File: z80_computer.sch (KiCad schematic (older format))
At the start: 14 parts, among them SW0 SW_Push, U0 Z80CPU, U1 CY62256NLL-55SNXI, U2 AT28C256_40PIN_ZIF, U4 SN74LS04N, U5 SN74LS00N, Y0 Crystal 6 MHZ

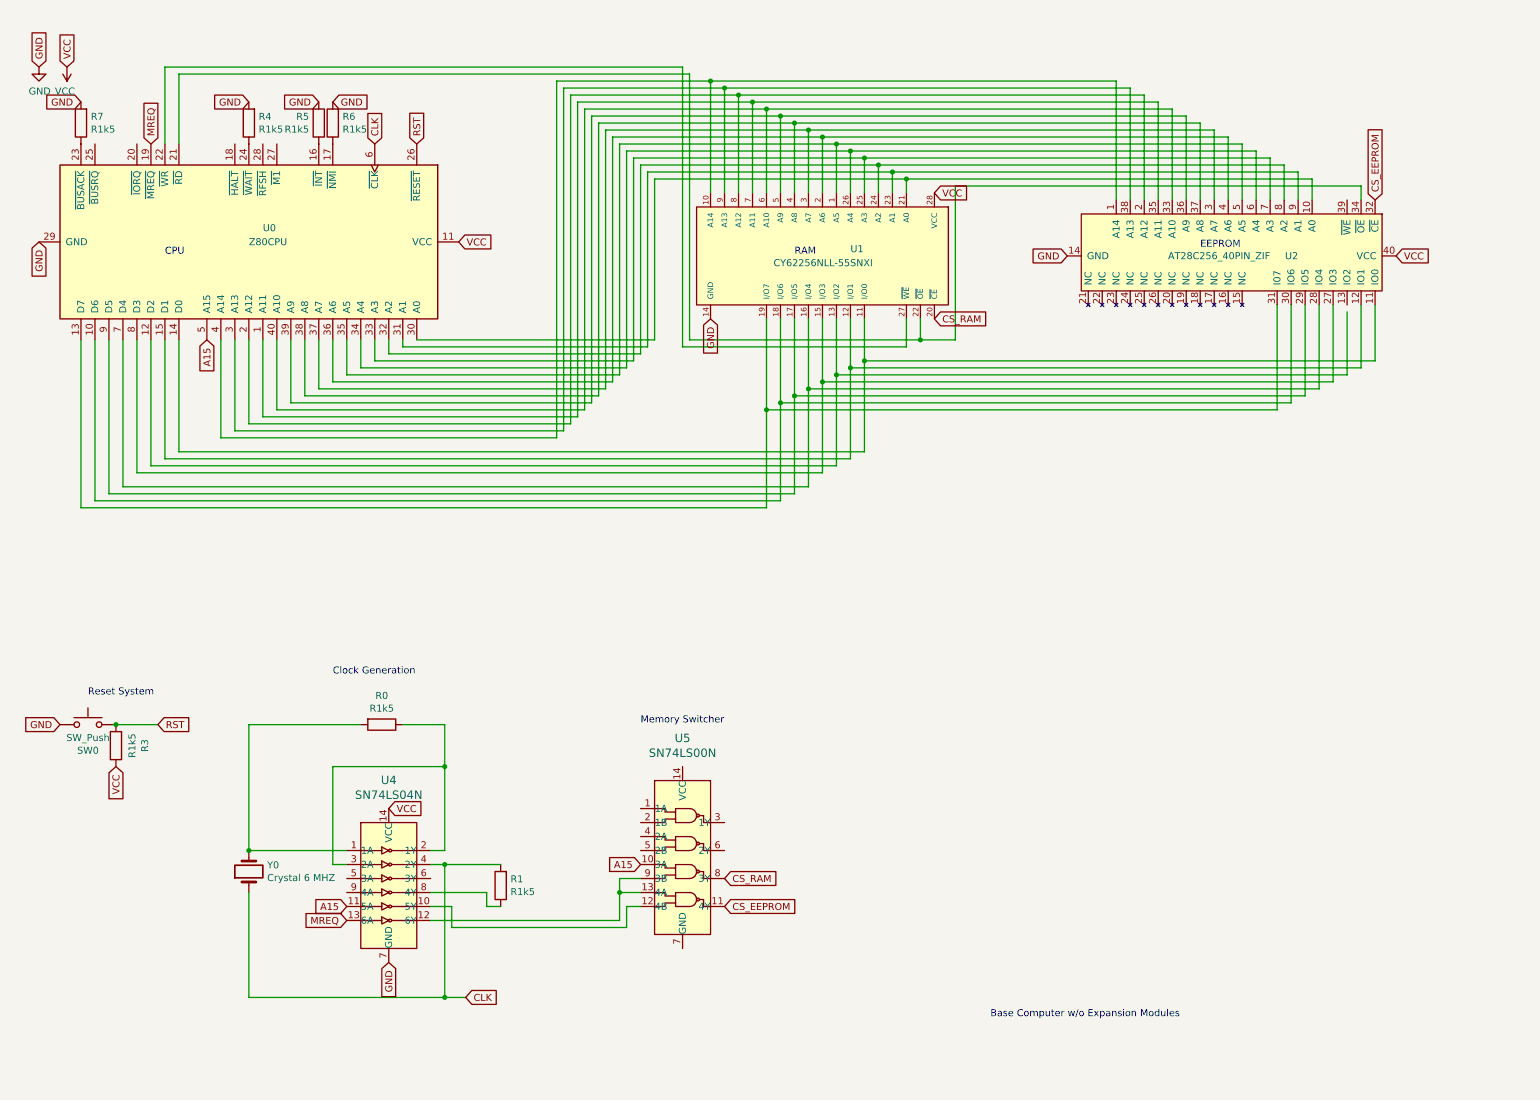
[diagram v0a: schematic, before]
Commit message: added second page on schematic detailing the debugging platform
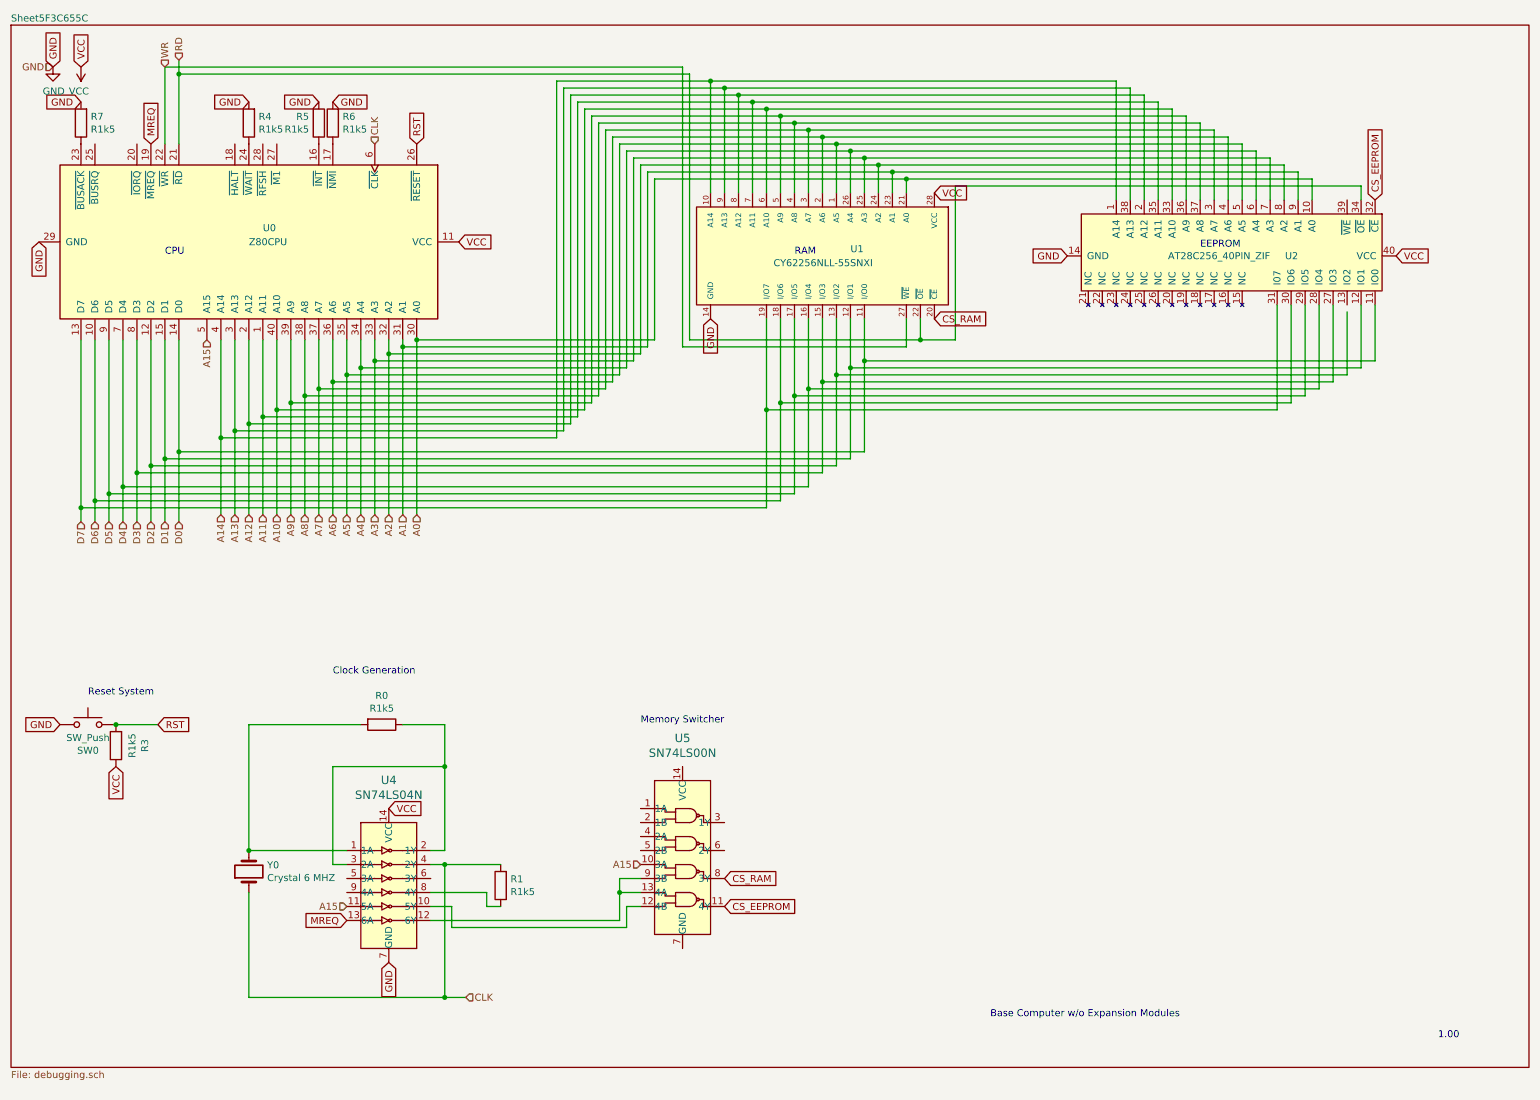
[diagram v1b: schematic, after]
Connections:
- net A14: now reaches U0.4 (A14), U1.10 (A14), U2.1 (A14)
- net A0: now reaches U0.30 (A0), U1.21 (A0), U2.10 (A0)
- net D0: now reaches U0.14 (D0), U1.11 (I/O0), U2.11 (IO0)
- net D1: now reaches U0.15 (D1), U1.12 (I/O1), U2.12 (IO1)
- net A12: now reaches U0.2 (A12), U1.8 (A12), U2.2 (A12)
- net D3: now reaches U0.8 (D3), U1.15 (I/O3), U2.27 (IO3)
- net D4: now reaches U0.7 (D4), U1.16 (I/O4), U2.28 (IO4)
- net D5: now reaches U0.9 (D5), U1.17 (I/O5), U2.29 (IO5)
- net A7: now reaches U0.37 (A7), U1.3 (A7), U2.3 (A7)
- net D6: now reaches U0.10 (D6), U1.18 (I/O6), U2.30 (IO6)
- net D7: now reaches U0.13 (D7), U1.19 (I/O7), U2.31 (I07)
- net A10: now reaches U0.40 (A10), U1.6 (A10), U2.33 (A10)
- net RD: now reaches U0.21 (~RD~), U1.22 (~OE~), U2.34 (~OE)
- net A11: now reaches U0.1 (A11), U1.7 (A11), U2.35 (A11)
- net A9: now reaches U0.39 (A9), U1.5 (A9), U2.36 (A9)
- net A8: now reaches U0.38 (A8), U1.4 (A8), U2.37 (A8)
- net A13: now reaches U0.3 (A13), U1.9 (A13), U2.38 (A13)
- net A6: now reaches U0.36 (A6), U1.2 (A6), U2.4 (A6)
- net A5: now reaches U0.35 (A5), U1.1 (A5), U2.5 (A5)
- net A4: now reaches U0.34 (A4), U1.26 (A4), U2.6 (A4)
- net A3: now reaches U0.33 (A3), U1.25 (A3), U2.7 (A3)
- net A2: now reaches U0.32 (A2), U1.24 (A2), U2.8 (A2)
- net A1: now reaches U0.31 (A1), U1.23 (A1), U2.9 (A1)
- net D2: now reaches U0.12 (D2), U1.13 (I/O2)
- net WR: now reaches U0.22 (~WR~), U1.27 (~WE~)
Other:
- note added: "1.00\n"
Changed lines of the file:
@@
 $Descr A4 11693 8268
 encoding utf-8
-Sheet 1 1
+Sheet 1 2
 Title ""
 Date ""
@@
 L power:GND #PWR?
 U 1 1 5F2413C5
-P 600 700
-F 0 "#PWR?" H 600 450 50  0001 C CNN
-F 1 "GND" H 605 527 50  0000 C CNN
-F 2 "" H 600 700 50  0001 C CNN
-F 3 "" H 600 700 50  0001 C CNN
-	1    600  700
+P 700 700
+F 0 "#PWR?" H 700 450 50  0001 C CNN
+F 1 "GND" H 705 527 50  0000 C CNN
+F 2 "" H 700 700 50  0001 C CNN
+F 3 "" H 700 700 50  0001 C CNN
+	1    700  700
 	1    0    0    -1
 $EndComp
-Text GLabel 600  700  1    50   Input ~ 0
+Text GLabel 700  700  1    50   Input ~ 0
 GND
 Wire Wire Line
@@
 L power:VCC #PWR?
 U 1 1 5F2D4698
-P 800 700
-F 0 "#PWR?" H 800 550 50  0001 C CNN
-F 1 "VCC" H 815 873 50  0000 C CNN
-F 2 "" H 800 700 50  0001 C CNN
-F 3 "" H 800 700 50  0001 C CNN
-	1    800  700
+P 900 700
+F 0 "#PWR?" H 900 550 50  0001 C CNN
+F 1 "VCC" H 915 873 50  0000 C CNN
+F 2 "" H 900 700 50  0001 C CNN
+F 3 "" H 900 700 50  0001 C CNN
+	1    900  700
 	-1   0    0    1
 $EndComp
-Text GLabel 800  700  1    50   Input ~ 0
+Text GLabel 900  700  1    50   Input ~ 0
 VCC
 Wire Wire Line
@@
 	1500 3500 1500 2650
 Connection ~ 6400 2850
-Wire Wire Line
-	1400 2650 1400 3550
 Wire Wire Line
 	1400 3550 6300 3550
@@
 	3650 7350 3500 7350
 Connection ~ 3500 7350
-Text GLabel 3650 7350 2    50   Input ~ 0
-CLK
-Text GLabel 3000 1250 1    50   Input ~ 0
-CLK
 Text Notes 2700 5050 0    50   ~ 0
 Clock Generation
@@
 	1    0    0    -1
 $EndComp
-Text GLabel 1800 2650 3    50   Input ~ 0
-A15
-Text GLabel 2800 6700 0    50   Input ~ 0
-A15
 Wire Wire Line
 	3400 6700 3550 6700
@@
 Text GLabel 10150 1650 1    50   Input ~ 0
 CS_EEPROM
-Text GLabel 4900 6400 0    50   Input ~ 0
-A15
 Text GLabel 2800 6800 0    50   Input ~ 0
 MREQ
@@
 Text Notes 1500 2050 0    50   ~ 0
 CPU
+Text HLabel 3000 1250 1    50   Input ~ 0
+CLK
+Text HLabel 3650 7350 2    50   Input ~ 0
+CLK
+Text HLabel 1800 2650 3    50   Input ~ 0
+A15
+Text HLabel 1900 3900 3    50   Input ~ 0
+A14
+Text HLabel 2000 3900 3    50   Input ~ 0
+A13
+Text HLabel 2100 3900 3    50   Input ~ 0
+A12
+Text HLabel 2200 3900 3    50   Input ~ 0
+A11
+Text HLabel 2300 3900 3    50   Input ~ 0
+A10
+Text HLabel 2400 3900 3    50   Input ~ 0
+A9
+Text HLabel 2500 3900 3    50   Input ~ 0
+A8
+Text HLabel 2600 3900 3    50   Input ~ 0
+A7
+Text HLabel 2700 3900 3    50   Input ~ 0
+A6
+Text HLabel 2800 3900 3    50   Input ~ 0
+A5
+Text HLabel 2900 3900 3    50   Input ~ 0
+A4
+Text HLabel 3000 3900 3    50   Input ~ 0
+A3
+Text HLabel 3100 3900 3    50   Input ~ 0
+A2
+Text HLabel 3200 3900 3    50   Input ~ 0
+A1
+Text HLabel 3300 3900 3    50   Input ~ 0
+A0
+Wire Wire Line
+	1900 3350 1900 3900
+Connection ~ 1900 3350
+Wire Wire Line
+	2000 3900 2000 3300
+Connection ~ 2000 3300
+Wire Wire Line
+	2100 3250 2100 3900
+Connection ~ 2100 3250
+Wire Wire Line
+	2200 3200 2200 3900
+Connection ~ 2200 3200
+Wire Wire Line
+	2300 3150 2300 3900
+Connection ~ 2300 3150
+Wire Wire Line
+	2400 3100 2400 3900
+Connection ~ 2400 3100
+Wire Wire Line
+	2500 3050 2500 3900
+Connection ~ 2500 3050
+Wire Wire Line
+	2600 3000 2600 3900
+Connection ~ 2600 3000
+Wire Wire Line
+	2700 2950 2700 3900
+Connection ~ 2700 2950
+Wire Wire Line
+	2800 2900 2800 3900
+Connection ~ 2800 2900
+Wire Wire Line
+	2900 2850 2900 3900
+Connection ~ 2900 2850
+Wire Wire Line
+	3000 2800 3000 3900
+Connection ~ 3000 2800
+Wire Wire Line
+	3100 2750 3100 3900
+Connection ~ 3100 2750
+Wire Wire Line
+	3200 2700 3200 3900
+Connection ~ 3200 2700
+Wire Wire Line
+	3300 2650 3300 3900
+Connection ~ 3300 2650
+Text HLabel 2800 6700 0    50   Input ~ 0
+A15
+Text HLabel 4900 6400 0    50   Input ~ 0
+A15
+Text HLabel 900  3950 3    50   Input ~ 0
+D7
+Text HLabel 1000 3950 3    50   Input ~ 0
+D6
+Text HLabel 1100 3950 3    50   Input ~ 0
+D5
+Text HLabel 1200 3950 3    50   Input ~ 0
+D4
+Text HLabel 1300 3950 3    50   Input ~ 0
+D3
+Text HLabel 1400 3950 3    50   Input ~ 0
+D2
+Text HLabel 1500 3950 3    50   Input ~ 0
+D1
+Text HLabel 1600 3950 3    50   Input ~ 0
+D0
+Wire Wire Line
+	900  3850 900  3950
+Connection ~ 900  3850
+Wire Wire Line
+	1000 3800 1000 3950
+Connection ~ 1000 3800
+Wire Wire Line
+	1100 3950 1100 3750
+Connection ~ 1100 3750
+Wire Wire Line
+	1200 3700 1200 3950
+Connection ~ 1200 3700
+Wire Wire Line
+	1300 3600 1300 3950
+Connection ~ 1300 3600
+Wire Wire Line
+	1400 2650 1400 3550
+Wire Wire Line
+	1400 3550 1400 3950
+Connection ~ 1400 3550
+Wire Wire Line
+	1500 3500 1500 3950
+Connection ~ 1500 3500
+Wire Wire Line
+	1600 3450 1600 3950
+Connection ~ 1600 3450
+Text HLabel 1500 700  1    50   Input ~ 0
+WR
+Text HLabel 1600 650  1    50   Input ~ 0
+RD
+Wire Wire Line
+	1600 750  1600 650
+Connection ~ 1600 750
+$Sheet
+S 400  400  10850 7450
+U 5F3C655D
+F0 "Sheet5F3C655C" 50
+F1 "debugging.sch" 50
+$EndSheet
+Text Notes 10600 7650 0    50   ~ 0
+1.00\n
+Text HLabel 700  700  0    50   Input ~ 0
+GND
 $EndSCHEMATC
